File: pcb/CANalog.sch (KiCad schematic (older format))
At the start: 73 parts, among them J1 USB_B_Micro, J2 PWR, J3 ESP_PROG, J5 AOUT, J6 DSUB9_Male, Q1 DMP3099L-7, Q2 MMBT2222A, SW1 SW_Push, SW2 SW_Push, U1 NUCLEO64-F302R8, U2 BL9342, U3 MCP6002-xSN, U4 SN65HVD230, U5 ESP-12E, U6 OPA330xxDBV, U7 74AHC1G66

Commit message: update to new circuitry, work in progress
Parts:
- removed C1: 1uF, Capacitor_SMD:C_0805_2012Metric, symbol Device:C
- removed C2: 0.1uF, Capacitor_SMD:C_0805_2012Metric, symbol Device:C
- removed D2, D6: SS14F, pl_Diode:SMAF, symbol Device:D_Schottky
- removed J6: DSUB9_Male, Connector_Dsub:DSUB-9_Male_Horizontal_P2.77x2.84mm_EdgePinOffset7.70mm_Housed_MountingHolesOffset9.12mm, symbol Connector:DB9_Male
- removed JP1, JP7, JP8: Jumper_3_Open, Connector_PinHeader_2.54mm:PinHeader_1x03_P2.54mm_Vertical, symbol Jumper:Jumper_3_Open
- removed JP2: TX_SELECT, Jumper:SolderJumper-3_P1.3mm_Bridged12_RoundedPad1.0x1.5mm, symbol Jumper:SolderJumper_3_Bridged12
- removed JP3: RX_SELECT, Jumper:SolderJumper-3_P1.3mm_Bridged12_RoundedPad1.0x1.5mm, symbol Jumper:SolderJumper_3_Bridged12
- removed R10, R11: 20k, Resistor_SMD:R_0805_2012Metric, symbol Device:R
- removed R7: 120k, Resistor_SMD:R_0805_2012Metric, symbol Device:R
- removed R8: 12k, Resistor_SMD:R_0805_2012Metric, symbol Device:R
- removed R9: 68k, Resistor_SMD:R_0805_2012Metric, symbol Device:R
- removed U1: NUCLEO64-F302R8, pl_Nucleo:nucleo-f302r8, symbol pl_nucleo64:NUCLEO64-F302R8
- removed U3: MCP6002-xSN, Package_SO:SOIC-8_3.9x4.9mm_P1.27mm, symbol Amplifier_Operational:MCP6002-xSN
- added C? (x4): 100nF, symbol Device:C
- added C? (x3): 1uF, symbol Device:C
- added C?: 0.1uF, Capacitor_SMD:C_0805_2012Metric, symbol Device:C
- added D?: SS14F, pl_Diode:SMAF, symbol Device:D_Schottky
- added FB? (x2): FBS, symbol Device:Ferrite_Bead_Small
- added J?: CAN, symbol Connector_Generic:Conn_01x03
- added JP?: NC, symbol Device:Jumper_NC_Small
- added Q?: DMP3099L-7, Package_TO_SOT_SMD:SOT-23, symbol Device:Q_PMOS_GSD
- added R? (x2): R, symbol Device:R
- added U?: STM32F302C8Tx, Package_QFP:LQFP-48_7x7mm_P0.5mm, symbol MCU_ST_STM32F3:STM32F302C8Tx
- added U?: MIC5504-3.3YM5, Package_TO_SOT_SMD:SOT-23-5, symbol Regulator_Linear:MIC5504-3.3YM5
- added U?: LMV321, symbol Amplifier_Operational:LMV321
- added Y?: Resonator, symbol Device:Resonator
- R19: value 23.7k -> 21k
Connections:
- net labels added: +BATT, 5V5, CAN_ACTIVITY, CAN_LED, ERROR, ERROR_LED, RXD, SPI_LED, SPI_TRANSFER, SWCLK, SWDIO, TXD, VDDA, XIN, XOUT
- net labels removed: AOUT0, AOUT1, DAC0, DAC1, DSUB_VIN, ESP_RX, ESP_TX, FTDI_RX, FTDI_TX, PB0, PC0, PC1, STM_RX, STM_TX
- wire segments 291 -> 278
- no-connect marks 58 -> 13
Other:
- note added: "3V3 LDO"
- note added: "5V5 DC-DC Converter"
- note added: "Analog Output Amplification"
- note added: "CAN Termination Selection"
- note added: "ESP8277 WiFi Interface"
- note added: "G = 5.0/3.3\nG = 1 + (68k/[120k + 12k])"
- note added: "Indicator LEDs"
- note added: "OPA330 Bypass Capacitors"
- note added: "Power Input with Polarity Protection"
- note added: "Rf"
- note added: "Rg"
- note added: "STM32F302 CAN Interface"
- note added: "STM32F302 Power Distribution and Bypass"
- note added: "USB Data and Power"
- note added: "USB Input Voltage Selection"
- note added: "Vfb = Vout * Rg/(Rf+Rg)\nRf = 124k for optimal response\nVfb = 0.794 typ"
- note removed: "AOUT Select"
- note removed: "Analog Output - General Purpose Op-Amp"
- note removed: "Analog Output - Precision Op-Amp"
- note removed: "CAN Terminal"
- note removed: "ESP Prog Header"
- note removed: "ESP UART Select"
- note removed: "External Power 5V Regulator"
- note removed: "External Power Input and Select"
- note removed: "G = 1 + (Rf/Rin)\nG = 5/3.3"
- note removed: "General Purpose Op-Amp - Unused and Bypass"
- note removed: "Nucleo-F302R8 Connector"
- note removed: "USB Port"
- note removed: "WiFi Interface"
- moved on the sheet: C10, C11, C5, C7, C8, C9, D1, D10, D4, D5, D8, D9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

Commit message: scematic additions
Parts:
- added C? (x2): 100nF, symbol Device:C
- added D?: D, symbol Device:D
- added H? (x4): MountingHole, symbol Mechanical:MountingHole
- added J?: SPI3, symbol Connector_Generic:Conn_01x06
- added J?: STM_PROG, symbol Connector_Generic:Conn_01x04
- added J?: I2C2, symbol Connector_Generic:Conn_01x04
- added JP?: NC, symbol Device:Jumper_NC_Small
- added TP?: PA3, symbol Connector:TestPoint
- R? (x2): Population (none) -> DNP
- Y?: value Resonator -> 16MHz; Population (none) -> DNP
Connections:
- net +5V: now also J?.1 (Pin_1), J?.1 (Pin_1)
- net GND: now also C?.1, C?.2, J?.4 (Pin_4), J?.4 (Pin_4), J?.6 (Pin_6), JP?.1; no longer C?.2, U?.8 (VSSA)
- net STM_RESET: now also C?.2, D?.2 (A)
- net SWCLK: now also J?.3 (Pin_3)
- net SWDIO: now also J?.2 (Pin_2)
- net PA3: now reaches U?.13 (PA3)
- net PA3: now also TP?.1
- net I2C_SCL: now reaches U?.30 (PA9)
- net I2C_SCL: now also J?.2 (Pin_2)
- net I2C_SDA: now reaches U?.31 (PA10)
- net I2C_SDA: now also J?.3 (Pin_3)
- net SPI3_CS: now reaches U?.38 (PA15)
- net SPI3_CS: now also J?.2 (Pin_2)
- net SPI3_SCK: now reaches U?.39 (PB3)
- net SPI3_SCK: now also J?.3 (Pin_3)
- net SPI3_MISO: now reaches U?.40 (PB4)
- net SPI3_MISO: now also J?.4 (Pin_4)
- net SPI3_MOSI: now reaches U?.41 (PB5)
- net SPI3_MOSI: now also J?.5 (Pin_5)
- net BOOT0: now reaches JP4.2, U?.44 (BOOT0)
- net RESET renamed ESP_RESET
- net ESP_RESET: now also C?.1, D?.1 (K)
- new net GNDA: C?.2, JP?.2, U?.8 (VSSA)
- no-connect marks 13 -> 18
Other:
- note added: "For Future 16bit DAC"
- moved on the sheet: C10, C9, C?, D1, D10, D8, D9, FB?, J1, J5, JP4, JP?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

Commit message: preliminary csv bom output
for inventory tracking
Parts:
- gave numbers to parts that had none: 33
- renumbered C4 to C1, C5 to C14, C9 to C16, C10 to C17, C3 to C18, C11 to C19, C6 to C4, C8 to C9, D3 to D1, D7 to D10, D4 to D2, D1 to D3, D8 to D6, D9 to D7, D10 to D8, D5 to D9, J2 to J1, J1 to J2, J3 to J6, J5 to J7, JP4 to JP3, R2 to R1, R19 to R10, R20 to R11, R6 to R12, R21 to R15, R14 to R16, R23 to R19, R3 to R2, R22 to R20, R24 to R21, R25 to R22, R26 to R23, R27 to R24, R12 to R25, R13 to R26, R4 to R3, R15 to R4, R16 to R5, R28 to R6, R5 to R7, R1 to R8, R18 to R9, U2 to U1, U4 to U8

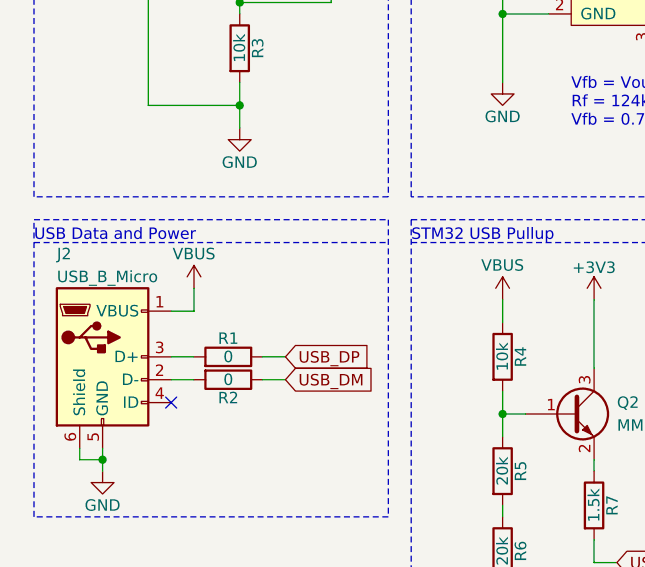
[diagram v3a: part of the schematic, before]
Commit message: add polyfuse on usb
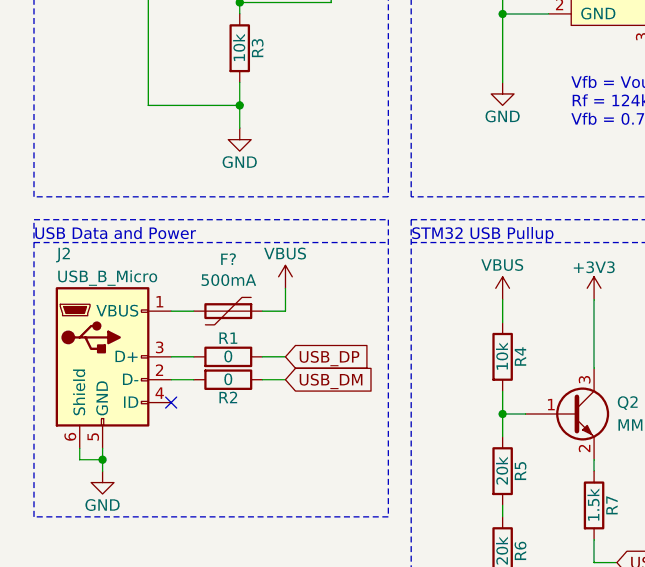
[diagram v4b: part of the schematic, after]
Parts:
- added F?: 500mA, symbol Device:Polyfuse
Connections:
- net VBUS: now also F?.1; no longer J2.1 (VBUS)
- new net: F?.2, J2.1 (VBUS)
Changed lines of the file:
@@
 L power:VBUS #PWR04
 U 1 1 60A975AF
-P 1300 2800
-F 0 "#PWR04" H 1300 2650 50  0001 C CNN
-F 1 "VBUS" H 1300 2950 50  0000 C CNN
-F 2 "" H 1300 2800 50  0001 C CNN
-F 3 "" H 1300 2800 50  0001 C CNN
-	1    1300 2800
-	1    0    0    -1
-$EndComp
-Wire Wire Line
-	1300 2800 1300 2900
+P 1700 2800
+F 0 "#PWR04" H 1700 2650 50  0001 C CNN
+F 1 "VBUS" H 1700 2950 50  0000 C CNN
+F 2 "" H 1700 2800 50  0001 C CNN
+F 3 "" H 1700 2800 50  0001 C CNN
+	1    1700 2800
+	1    0    0    -1
+$EndComp
 Wire Wire Line
 	1300 2900 1200 2900
@@
 	1    0    0    -1
 $EndComp
+$Comp
+L Device:Polyfuse F?
+U 1 1 60630AA9
+P 1450 2900
+F 0 "F?" V 1225 2900 50  0000 C CNN
+F 1 "500mA" V 1316 2900 50  0000 C CNN
+F 2 "" H 1500 2700 50  0001 L CNN
+F 3 "~" H 1450 2900 50  0001 C CNN
+	1    1450 2900
+	0    1    1    0
+$EndComp
+Wire Wire Line
+	1600 2900 1700 2900
+Wire Wire Line
+	1700 2900 1700 2800
 $EndSCHEMATC

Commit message: clear capacitor footprints
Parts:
- C1, C14, C17, C7: footprint Capacitor_SMD:C_0805_2012Metric -> (none)
- C12, C16, C18, C19, C4: value 0.1uF -> 100nF; footprint Capacitor_SMD:C_0805_2012Metric -> (none)
- C9: footprint Capacitor_SMD:C_0603_1608Metric -> (none)
- gave numbers to parts that had none: 1
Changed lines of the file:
@@
 P 14250 950
 F 0 "C18" H 14275 1050 50  0000 L CNN
-F 1 "0.1uF" H 14275 850 50  0000 L CNN
-F 2 "Capacitor_SMD:C_0805_2012Metric" H 14288 800 50  0001 C CNN
+F 1 "100nF" H 14275 850 50  0000 L CNN
+F 2 "" H 14288 800 50  0001 C CNN
 F 3 "~" H 14250 950 50  0001 C CNN
 	1    14250 950
@@
 P 15700 2900
 F 0 "C19" H 15725 3000 50  0000 L CNN
-F 1 "0.1uF" H 15725 2800 50  0000 L CNN
-F 2 "Capacitor_SMD:C_0805_2012Metric" H 15738 2750 50  0001 C CNN
+F 1 "100nF" H 15725 2800 50  0000 L CNN
+F 2 "" H 15738 2750 50  0001 C CNN
 F 3 "~" H 15700 2900 50  0001 C CNN
 	1    15700 2900
@@
 F 0 "C1" H 2675 1450 50  0000 L CNN
 F 1 "4.7uF" H 2675 1250 50  0000 L CNN
-F 2 "Capacitor_SMD:C_0805_2012Metric" H 2688 1200 50  0001 C CNN
+F 2 "" H 2688 1200 50  0001 C CNN
 F 3 "~" H 2650 1350 50  0001 C CNN
 	1    2650 1350
@@
 F 0 "C7" H 4725 1450 50  0000 L CNN
 F 1 "10uF" H 4725 1250 50  0000 L CNN
-F 2 "Capacitor_SMD:C_0805_2012Metric" H 4738 1200 50  0001 C CNN
+F 2 "" H 4738 1200 50  0001 C CNN
 F 3 "~" H 4700 1350 50  0001 C CNN
 	1    4700 1350
@@
 F 0 "C9" H 5275 1450 50  0000 L CNN
 F 1 "33pF" H 5275 1250 50  0000 L CNN
-F 2 "Capacitor_SMD:C_0603_1608Metric" H 5288 1200 50  0001 C CNN
+F 2 "" H 5288 1200 50  0001 C CNN
 F 3 "~" H 5250 1350 50  0001 C CNN
 	1    5250 1350
@@
 P 3850 1350
 F 0 "C4" H 3875 1450 50  0000 L CNN
-F 1 "0.1uF" H 3875 1250 50  0000 L CNN
-F 2 "Capacitor_SMD:C_0805_2012Metric" H 3888 1200 50  0001 C CNN
+F 1 "100nF" H 3875 1250 50  0000 L CNN
+F 2 "" H 3888 1200 50  0001 C CNN
 F 3 "~" H 3850 1350 50  0001 C CNN
 	1    3850 1350
@@
 P 6950 1400
 F 0 "C12" H 6975 1500 50  0000 L CNN
-F 1 "0.1uF" H 6975 1300 50  0000 L CNN
-F 2 "Capacitor_SMD:C_0805_2012Metric" H 6988 1250 50  0001 C CNN
+F 1 "100nF" H 6975 1300 50  0000 L CNN
+F 2 "" H 6988 1250 50  0001 C CNN
 F 3 "~" H 6950 1400 50  0001 C CNN
 	1    6950 1400
@@
 F 0 "C14" H 8175 5350 50  0000 L CNN
 F 1 "10uF" H 8175 5150 50  0000 L CNN
-F 2 "Capacitor_SMD:C_0805_2012Metric" H 8188 5100 50  0001 C CNN
+F 2 "" H 8188 5100 50  0001 C CNN
 F 3 "~" H 8150 5250 50  0001 C CNN
 	1    8150 5250
@@
 F 0 "C17" H 12775 8050 50  0000 L CNN
 F 1 "1uF" H 12775 7850 50  0000 L CNN
-F 2 "Capacitor_SMD:C_0805_2012Metric" H 12788 7800 50  0001 C CNN
+F 2 "" H 12788 7800 50  0001 C CNN
 F 3 "~" H 12750 7950 50  0001 C CNN
 	1    12750 7950
@@
 P 12350 7950
 F 0 "C16" H 12375 8050 50  0000 L CNN
-F 1 "0.1uF" H 12375 7850 50  0000 L CNN
-F 2 "Capacitor_SMD:C_0805_2012Metric" H 12388 7800 50  0001 C CNN
+F 1 "100nF" H 12375 7850 50  0000 L CNN
+F 2 "" H 12388 7800 50  0001 C CNN
 F 3 "~" H 12350 7950 50  0001 C CNN
 	1    12350 7950
@@
 $EndComp
 $Comp
-L Device:Polyfuse F?
+L Device:Polyfuse F1
 U 1 1 60630AA9
 P 1450 2900
-F 0 "F?" V 1225 2900 50  0000 C CNN
+F 0 "F1" V 1225 2900 50  0000 C CNN
 F 1 "500mA" V 1316 2900 50  0000 C CNN
 F 2 "" H 1500 2700 50  0001 L CNN

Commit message: start updating part details
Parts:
- removed D5: D, symbol Device:D
- removed D9: 1N4148, Diode_THT:D_DO-35_SOD27_P7.62mm_Horizontal, symbol Device:D
- added D5, D9: SS14F, pl_Diode:SMAF, symbol Device:D_Schottky
- C1, C14, C7: footprint (none) -> C_0805_2012Metric
- C10, C11, C12, C13, C15, C16, C17, C18, C19, C2, C3, C4, C5, C6, C8, C9: footprint (none) -> C_0603_1608Metric
- H1, H2, H3, H4: footprint (none) -> MountingHole:MountingHole_2.7mm_M2.5
- J3: footprint (none) -> Connector_PinHeader_2.54mm:PinHeader_1x06_P2.54mm_Vertical
- J4, J5: footprint (none) -> Connector_PinHeader_2.54mm:PinHeader_1x04_P2.54mm_Vertical
- J6, JP3: Population (none) -> DNP
- R1, R10, R11, R12, R15, R16, R17, R2, R22, R23, R24, R25, R26, R3, R4, R5, R6, R7, R8, R9: footprint Resistor_SMD:R_0805_2012Metric -> (none)
- R19, R20, R21: footprint Resistor_SMD:R_0805_2012Metric -> Resistor_SMD:R_0603_1608Metric
- SW1, SW2: footprint Button_Switch_THT:SW_PUSH_6mm -> (none)
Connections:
- net ESP_RESET: now also D5.1 (K)
- net RXD: now also D9.2 (A)
- net STM_RESET: now also D5.2 (A)
- net at J6.3 (Pin_3): now also D9.1 (K)

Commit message: adding details
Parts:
- D10: value PESD1CAN-UX -> PESD1CAN; footprint Package_TO_SOT_SMD:SOT-323_SC-70 -> Package_TO_SOT_SMD:SOT-23; MPN (none) -> PESD1CAN; Manufacture (none) -> TECH PUBLIC; SPN (none) -> C907838; Supplier (none) -> LCSC; Supplier Link (none) -> https://lcsc.com/product-detail/Diodes-ESD_TECH-PUBLIC-PESD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
- D2, D4: MPN (none) -> SS14F; Manufacture (none) -> Shandong Jingdao Microelectronics; SPN (none) -> C108832; Supplier (none) -> LCSC; Supplier Link (none) -> https://lcsc.com/product-detail/Schottky-Barrier-Diodes-SBD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
- D5, D9: value SS14F -> 1N4148W; footprint pl_Diode:SMAF -> Diode_SMD:D_SOD-123; MPN (none) -> 1N4148W; Manufacture (none) -> Microdiode Electronics; SPN (none) -> C84367; Supplier (none) -> LCSC; Supplier Link (none) -> https://lcsc.com/product-detail/Switching-Diode_MDD-Microdi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
- F1: footprint (none) -> Fuse:Fuse_0603_1608Metric_Castellated; MPN (none) -> MF-FSMF050X-2; Manufacture (none) -> Bourns; SPN (none) -> C210357; Supplier (none) -> LCSC; Supplier Link (none) -> https://lcsc.com/product-detail/Surface-Mount-Fuses_BOURNS_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
- FB1, FB2: footprint (none) -> Inductor_SMD:L_0603_1608Metric; MPN (none) -> CBG160808U070T; Manufacture (none) -> FH(Guangdong Fenghua Advanced Tech); SPN (none) -> C98494; Supplier (none) -> LCSC; Supplier Link (none) -> https://lcsc.com/product-detail/Ferrite-Beads_FH-Guangdong-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
- J2: footprint Connector_USB:USB_Micro-B_Amphenol_10103594-0001LF_Horizontal -> (none)
- R1, R2: footprint (none) -> Resistor_SMD:R_0603_1608Metric; MPN (none) -> RC0603JR-070RL; Manufacture (none) -> YAGEO; SPN (none) -> C95177; Supplier (none) -> LCSC; Supplier Link (none) -> https://lcsc.com/product-detail/Chip-Resistor-Surface-Mount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
- R10: value 21k -> 20.5k; footprint (none) -> Resistor_SMD:R_0603_1608Metric; MPN (none) -> 0603WAD2052T5E; Manufacture (none) -> UNI-ROYAL(Uniroyal Elec); SPN (none) -> C423063; Supplier (none) -> LCSC; Supplier Link (none) -> https://lcsc.com/product-detail/Chip-Resistor-Surface-Mount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
- R11, R13, R14, R22, R23, R24, R8: footprint (none) -> Resistor_SMD:R_0603_1608Metric
- R12, R15, R16, R17, R18, R3, R4: footprint (none) -> Resistor_SMD:R_0603_1608Metric; MPN (none) -> RC0603JR-0710KL; Manufacture (none) -> YAGEO; SPN (none) -> C99198; Supplier (none) -> LCSC; Supplier Link (none) -> https://lcsc.com/product-detail/Chip-Resistor-Surface-Mount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
- R19: MPN (none) -> RT0603BRD07120KL; Manufacture (none) -> YAGEO; SPN (none) -> C705720; Supplier (none) -> LCSC; Supplier Link (none) -> https://lcsc.com/product-detail/Chip-Resistor-Surface-Mount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
- R20: MPN (none) -> RT0603BRD0712KL; Manufacture (none) -> YAGEO; SPN (none) -> C326735; Supplier (none) -> LCSC; Supplier Link (none) -> https://lcsc.com/product-detail/Chip-Resistor-Surface-Mount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
- R21: MPN (none) -> RT0603BRD0768KL; Manufacture (none) -> YAGEO; SPN (none) -> C705793; Supplier (none) -> LCSC; Supplier Link (none) -> https://lcsc.com/product-detail/Chip-Resistor-Surface-Mount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
- R25: footprint (none) -> Resistor_SMD:R_0603_1608Metric; Population (none) -> DNP
- R26: footprint (none) -> Resistor_SMD:R_0603_1608Metric; MPN (none) -> RS-03K1200FT; Manufacture (none) -> FH(Guangdong Fenghua Advanced Tech); SPN (none) -> C310266; Supplier (none) -> LCSC; Supplier Link (none) -> https://lcsc.com/product-detail/Chip-Resistor-Surface-Mount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
- R5, R6: footprint (none) -> Resistor_SMD:R_0603_1608Metric; MPN (none) -> 0603WAJ0203T5E; Manufacture (none) -> UNI-ROYAL(Uniroyal Elec); SPN (none) -> C25586; Supplier (none) -> LCSC; Supplier Link (none) -> https://lcsc.com/product-detail/Chip-Resistor-Surface-Mount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
- R7: footprint (none) -> Resistor_SMD:R_0603_1608Metric; MPN (none) -> RS-03K152JT; Manufacture (none) -> FH(Guangdong Fenghua Advanced Tech); SPN (none) -> C118361; Supplier (none) -> LCSC; Supplier Link (none) -> https://lcsc.com/product-detail/Chip-Resistor-Surface-Mount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
- R9: footprint (none) -> Resistor_SMD:R_0603_1608Metric; MPN (none) -> 0603WAF1243T5E; Manufacture (none) -> UNI-ROYAL(Uniroyal Elec); SPN (none) -> C22788; Supplier (none) -> LCSC; Supplier Link (none) -> https://lcsc.com/product-detail/Chip-Resistor-Surface-Mount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
- U3: value STM32F302C8Tx -> STM32F302C8T6; MPN (none) -> STM32F302C8T6; Manufacture (none) -> STMicroelectronics; SPN (none) -> 511-STM32F302C8T6; Supplier (none) -> Mouser; Supplier Link (none) -> https://www.mouser.com/ProductDetail/511-STM32F302C8T6
- U6: MPN (none) -> OPA330AIDBVR; Manufacture (none) -> Texas Instruments; SPN (none) -> C38649; Supplier (none) -> LCSC; Supplier Link (none) -> https://lcsc.com/product-detail/Precision-OpAmps_Texas-Inst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
- U7: MPN (none) -> 74AHC1G66GW,125; Manufacture (none) -> Nexperia; SPN (none) -> C96224; Supplier (none) -> LCSC; Supplier Link (none) -> https://lcsc.com/product-detail/Analog-Switches_Nexperia-74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
- U8: MPN (none) -> SN65HVD230DR; Manufacture (none) -> Texas Instruments; SPN (none) -> C12084; Supplier (none) -> LCSC; Supplier Link (none) -> https://lcsc.com/product-detail/CAN-ICs_Texas-Instruments-S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
- Y1: MPN (none) -> CSTNE16M0VH3C000R0; Manufacture (none) -> Murata Electronics; SPN (none) -> 81-CSTNE16M0VH3C000R; Supplier (none) -> Mouser; Supplier Link (none) -> https://www.mouser.com/ProductDetail/81-CSTNE16M0VH3C000R
